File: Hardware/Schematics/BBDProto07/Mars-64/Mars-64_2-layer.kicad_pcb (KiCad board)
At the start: 2 copper layers, 45.7 x 101.6 mm, 79 parts, among them J101 Conn_Coaxial, J102 Conn_Coaxial, U101 ADG731, U102 ADG731

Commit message: Added some design elemets to the board
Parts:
- removed PmodF2: Conn_02x06_Top_Bottom, Mars-64:PinHeader_2x06_P2.54mm_Vertical_SMD_TopBottom_Mirrored
- removed PmodM1: Conn_02x06_Top_Bottom, Mars-64:PinHeader_2x06_P2.54mm_Vertical_SMD_TopBottom
- added G***: LOGO, Mars-64:BBD_Logo_33x33mm, F.Cu at (78.7, 61.0)
- added PmodF: Conn_02x06_Top_Bottom, Mars-64:PinHeader_2x06_P2.54mm_Vertical_SMD_TopBottom, B.Cu at (68.6, 53.3)
- added PmodM: Conn_02x06_Top_Bottom, Mars-64:PinHeader_2x06_P2.54mm_Vertical_SMD_TopBottom_Mirrored, B.Cu at (94.0, 53.3)
- H1, H2, H3, H4: footprint MountingHole:MountingHole_2.2mm_M2 -> MountingHole:MountingHole_2.7mm_M2.5
- moved H1 7.73 mm to (59.7, 68.6)
- moved H2 7.73 mm to (97.8, 68.6)
- moved JA 7.62 mm to (94.0, 76.2)
- moved C1 4.02 mm to (64.8, 64.8)
- moved JP4 3.59 mm to (63.5, 73.7)
- moved JB 2.54 mm to (94.0, 137.2)
- moved H3 1.27 mm to (59.7, 127.0)
- moved H4 1.27 mm to (97.8, 127.0)
- moved TPAGND1 1.27 mm to (64.8, 76.2)
- renumbered J101 to JA, J102 to JB
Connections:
- net Net-(JP5-Pad2) renamed /VSS
- U101 pad 15: (no net) -> Net-(U101-Pad15)
- U101 pad 16: (no net) -> Net-(U101-Pad16)
- U101 pad 20: (no net) -> Net-(U101-Pad20)
- U101 pad 21: (no net) -> Net-(U101-Pad21)
- U101 pad 22: (no net) -> Net-(U101-Pad22)
- U101 pad 41: (no net) -> Net-(U101-Pad41)
- U101 pad 42: (no net) -> Net-(U101-Pad42)
- U101 pad 44: (no net) -> Net-(U101-Pad44)
- U102 pad 15: (no net) -> Net-(U102-Pad15)
- U102 pad 16: (no net) -> Net-(U102-Pad16)
- U102 pad 20: (no net) -> Net-(U102-Pad20)
- U102 pad 21: (no net) -> Net-(U102-Pad21)
- U102 pad 22: (no net) -> Net-(U102-Pad22)
- U102 pad 41: (no net) -> Net-(U102-Pad41)
- U102 pad 42: (no net) -> Net-(U102-Pad42)
- U102 pad 44: (no net) -> Net-(U102-Pad44)
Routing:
- net /VSS: track 204.3 -> 0.00 mm
- net /VCC3V3: track 184.6 -> 0.00 mm, vias 4 -> 0
- net /SPI_CLK: track 184.0 -> 0.00 mm, vias 2 -> 0
- net GND: track 170.6 -> 0.00 mm, vias 2 -> 0
- net /SPI_MOSI: track 139.6 -> 0.00 mm
- net /~SPI_CE: track 134.1 -> 0.00 mm
- net Net-(J101-Pad2): track 124.4 -> 0.00 mm, vias 2 -> 0
- net /DB: track 108.6 -> 0.00 mm, vias 2 -> 0
- net Net-(TP204-Pad1): track 65.9 -> 0.00 mm
- net /AGND: track 61.8 -> 0.00 mm, vias 3 -> 1
- net Net-(TP210-Pad1): track 61.2 -> 0.00 mm
- net Net-(TP131-Pad1): track 60.8 -> 0.00 mm, vias 2 -> 1
- net Net-(TP205-Pad1): track 59.1 -> 0.00 mm
- net Net-(TP132-Pad1): track 58.3 -> 0.00 mm
- net Net-(TP208-Pad1): track 56.4 -> 0.00 mm
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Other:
- board text added: "3V3"
- board text added: "AGND"
- board text added: "BBD Mars-64 rev. E"
- board text added: "DA"
- board text added: "DB"
- board text added: "GND"
- board text added: "SPI_CE"
- board text added: "SPI_CLK"
- board text added: "SPI_MOSI"
- board text added: "TP11"
- board text added: "TP18"
- board text added: "TP41"
- board text added: "TP48"
- board text added: "TP51"
- board text added: "TP58"
- board text added: "TP81"
- board text added: "TP88"
- board text added: "VSS"
- board text removed: "BBD Mars-64 rev. D"

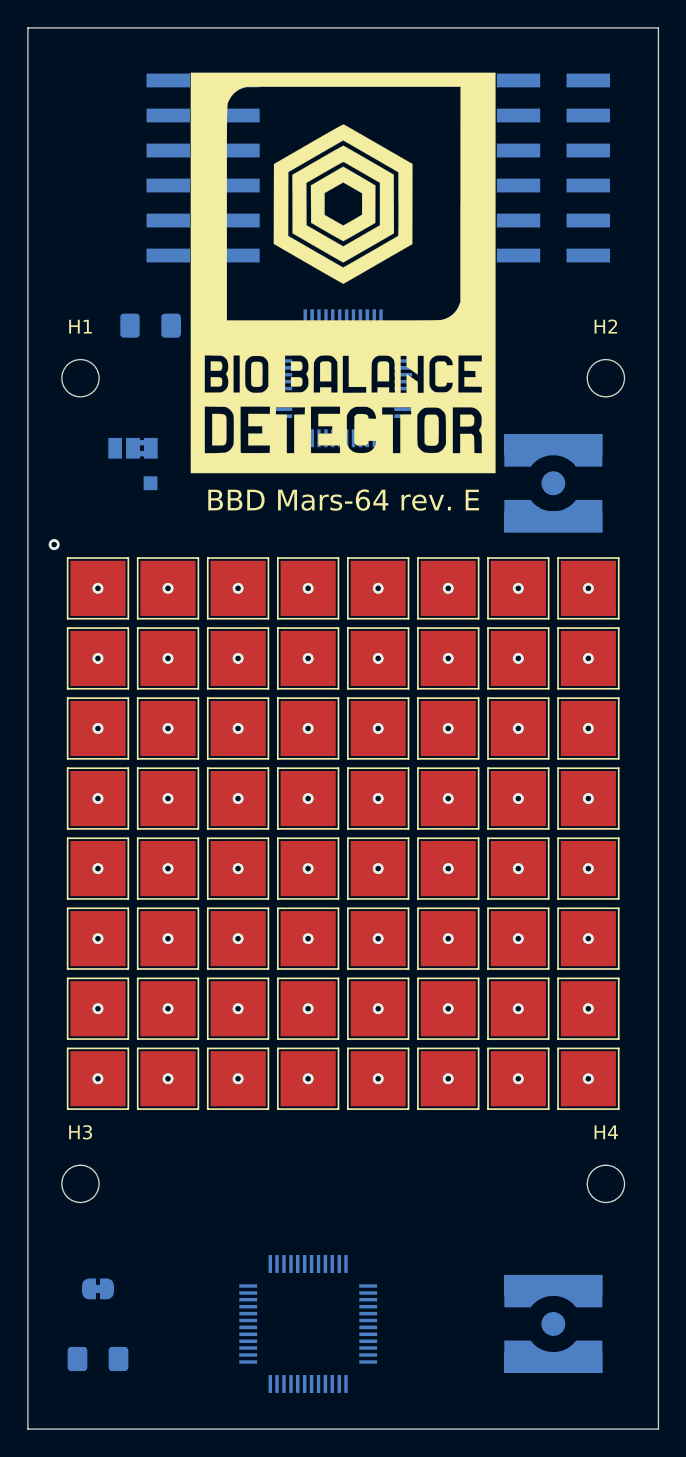
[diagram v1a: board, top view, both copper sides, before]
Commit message: Updated the 2-layer PCB, preprared it for manufacturing
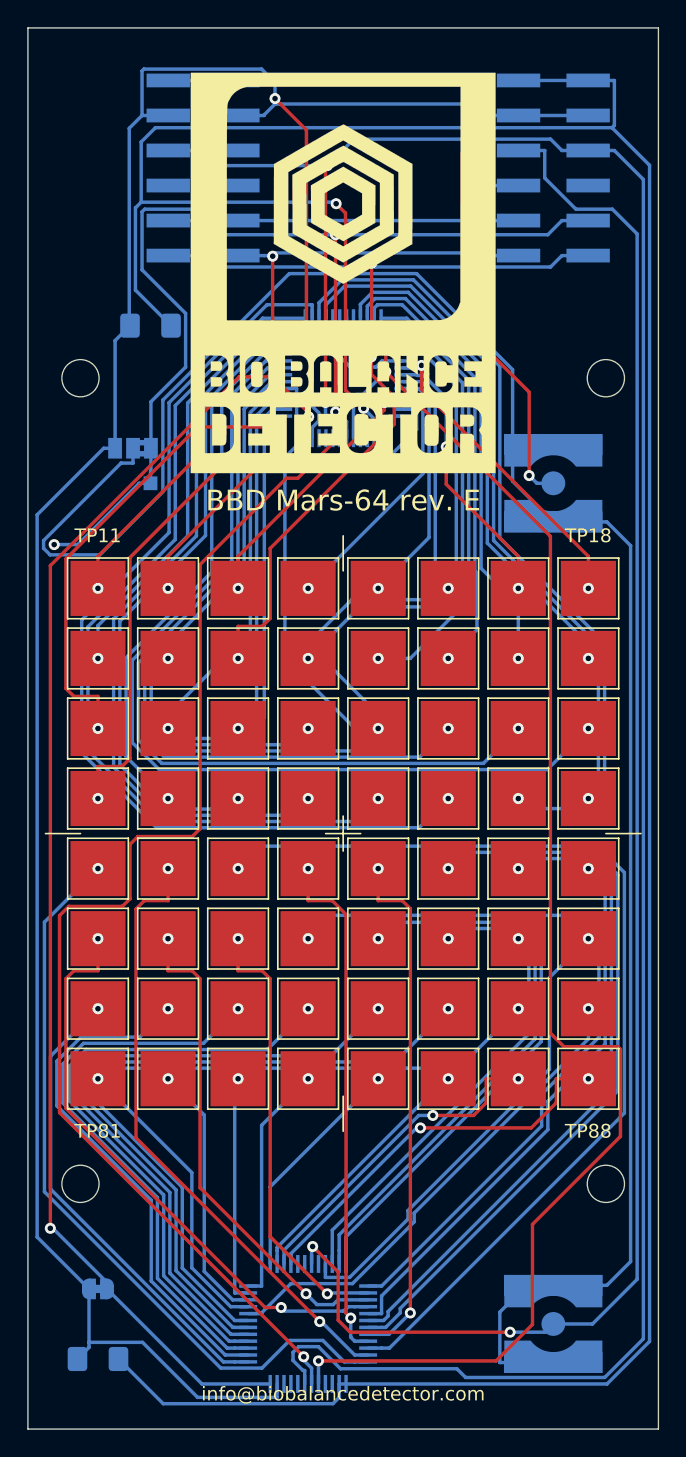
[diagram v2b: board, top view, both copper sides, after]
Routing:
- net /VCC3V3: track 0.00 -> 233.3 mm, vias 0 -> 2
- net GND: track 0.00 -> 181.1 mm, vias 0 -> 2
- net /SPI_CLK: track 0.00 -> 171.9 mm, vias 0 -> 2
- net Net-(J101-Pad2): track 0.00 -> 151.9 mm
- net /~SPI_CE: track 0.00 -> 144.8 mm, vias 0 -> 3
- net /SPI_MOSI: track 0.00 -> 137.9 mm, vias 0 -> 3
- net /VSS: track 0.00 -> 125.7 mm, vias 0 -> 3
- net /DB: track 0.00 -> 119.1 mm, vias 0 -> 2
- net Net-(TP203-Pad1): track 0.00 -> 72.6 mm
- net Net-(TP130-Pad1): track 0.00 -> 72.0 mm
- net Net-(TP124-Pad1): track 0.00 -> 67.5 mm
- net Net-(TP110-Pad1): track 0.00 -> 67.3 mm
- net Net-(TP129-Pad1): track 0.00 -> 63.6 mm
- net Net-(TP123-Pad1): track 0.00 -> 60.7 mm
- net Net-(TP131-Pad1): track 0.00 -> 58.8 mm
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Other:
- board text added: "info@biobalancedetector.com"
